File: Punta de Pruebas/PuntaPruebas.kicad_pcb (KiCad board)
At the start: 2 copper layers, 61 x 38.1 mm, 23 parts, among them P1 CONN_2, P2 CONN_1, P3 CONN_1, SW1 Llave Inversora, U1 40106

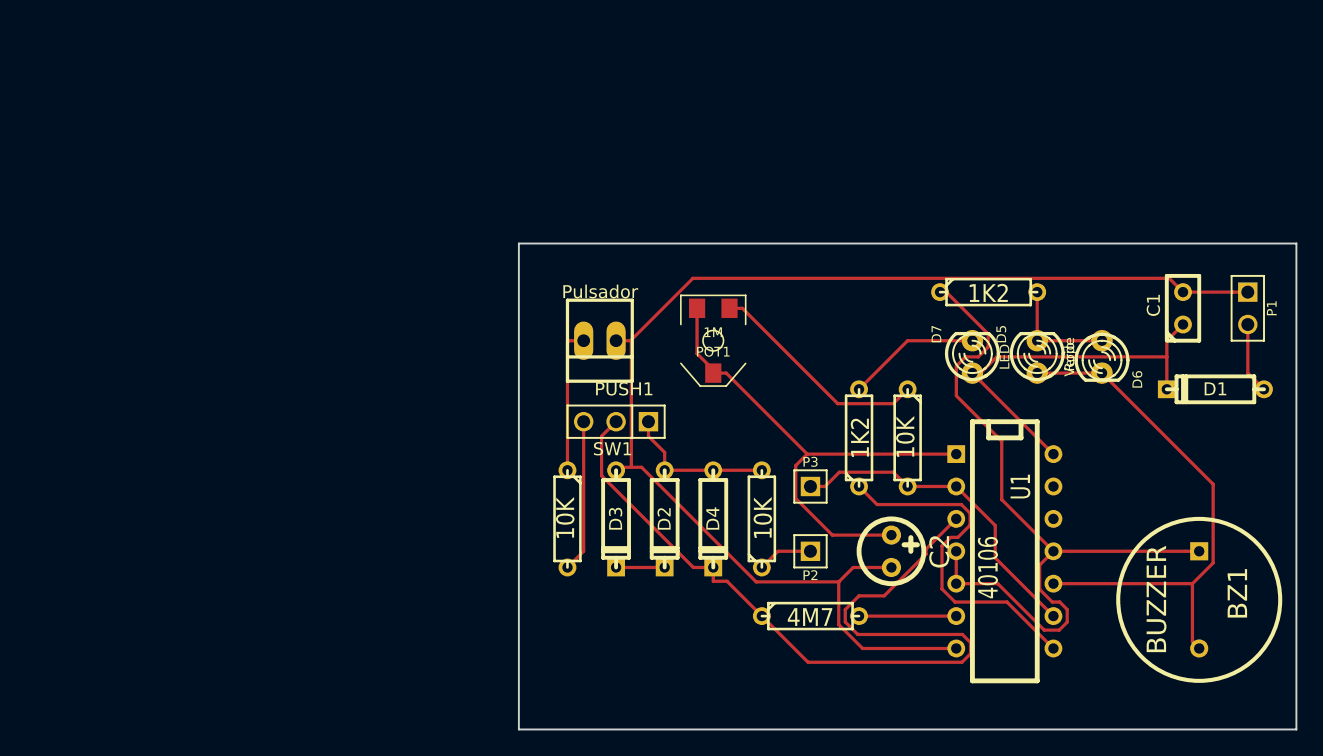
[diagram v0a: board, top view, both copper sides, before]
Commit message: Realizo un layout alternativo del PCB, haciendo más claro el ensamblado
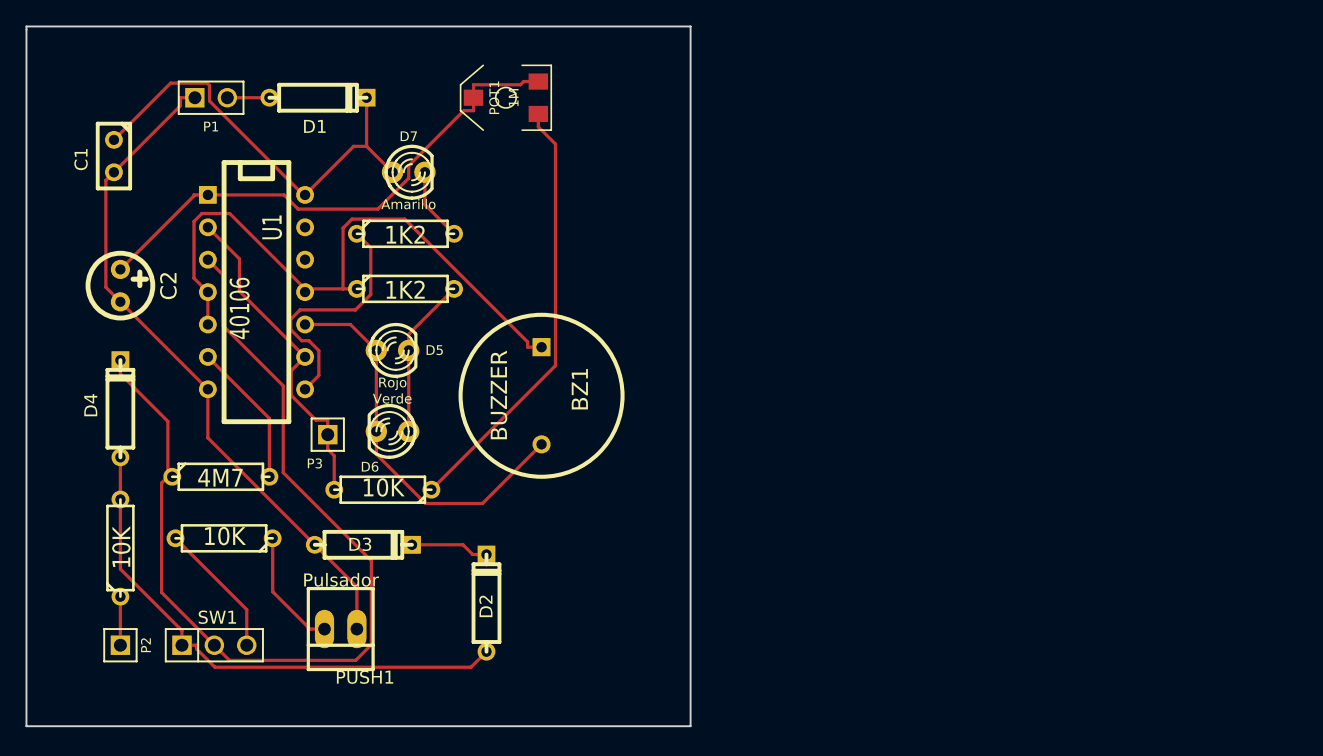
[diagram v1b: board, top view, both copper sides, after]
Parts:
- C2: value CAPAPOL -> 1 uF
- D7: value LED -> Amarillo
- moved C1 84.7 mm to (141.0, 126.5), turned to 270 degrees
- moved P1 82.9 mm to (148.6, 121.9), turned to 0 degrees
- moved D1 74.0 mm to (157.0, 121.9), turned to 0 degrees
- moved C2 63.9 mm to (141.5, 136.7)
- moved U1 62.1 mm to (152.1, 137.2)
- moved D6 55.9 mm to (162.8, 148.1), turned to 180 degrees
- moved P2 54.6 mm to (141.5, 164.8), turned to 270 degrees
- moved BZ1 54.0 mm to (174.5, 145.3)
- moved D5 50.5 mm to (162.8, 141.7), turned to 0 degrees
- moved R1 50.3 mm to (141.5, 157.2)
- moved R4 47.5 mm to (149.4, 151.6)
- moved D4 47.3 mm to (141.5, 146.3), turned to 90 degrees
- moved D7 46.5 mm to (164.1, 127.8), turned to 0 degrees
- moved R5 45.7 mm to (163.8, 136.9)
- moved R3 41.3 mm to (162.1, 152.7), turned to 180 degrees
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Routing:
- net VSS: track 101.2 -> 53.4 mm
- net N-000006: track 12.0 -> 42.0 mm
- net N-0000014: track 17.5 -> 34.1 mm
- net N-000003: track 42.1 -> 31.0 mm
- net N-000008: track 64.8 -> 75.0 mm
- net N-000002: track 58.6 -> 49.3 mm
- net N-0000015: track 27.4 -> 19.5 mm
- net N-0000017: track 10.5 -> 5.77 mm
- net VDD: track 30.1 -> 34.3 mm
- net N-000009: track 7.62 -> 11.4 mm
- net N-000001: track 8.89 -> 12.6 mm
- net N-000004: track 3.81 -> 6.16 mm
- net N-000007: track 5.61 -> 3.30 mm
- net N-0000011: track 11.4 -> 9.46 mm
- net N-0000013: track 39.9 -> 41.6 mm
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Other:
- board size 61 x 38.1 mm -> 52.1 x 54.9 mm
